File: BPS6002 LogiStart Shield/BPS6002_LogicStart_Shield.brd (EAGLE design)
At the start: 118.4 x 58.7 mm, 84 parts, among them J1 AUDIO-CONNECTOR-6P-SMD-344003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, Q1 MMBTA56, Q2 MMBTA56, Q3 MMBTA56, Q4 MMBTA56, Q5 MMBTA56

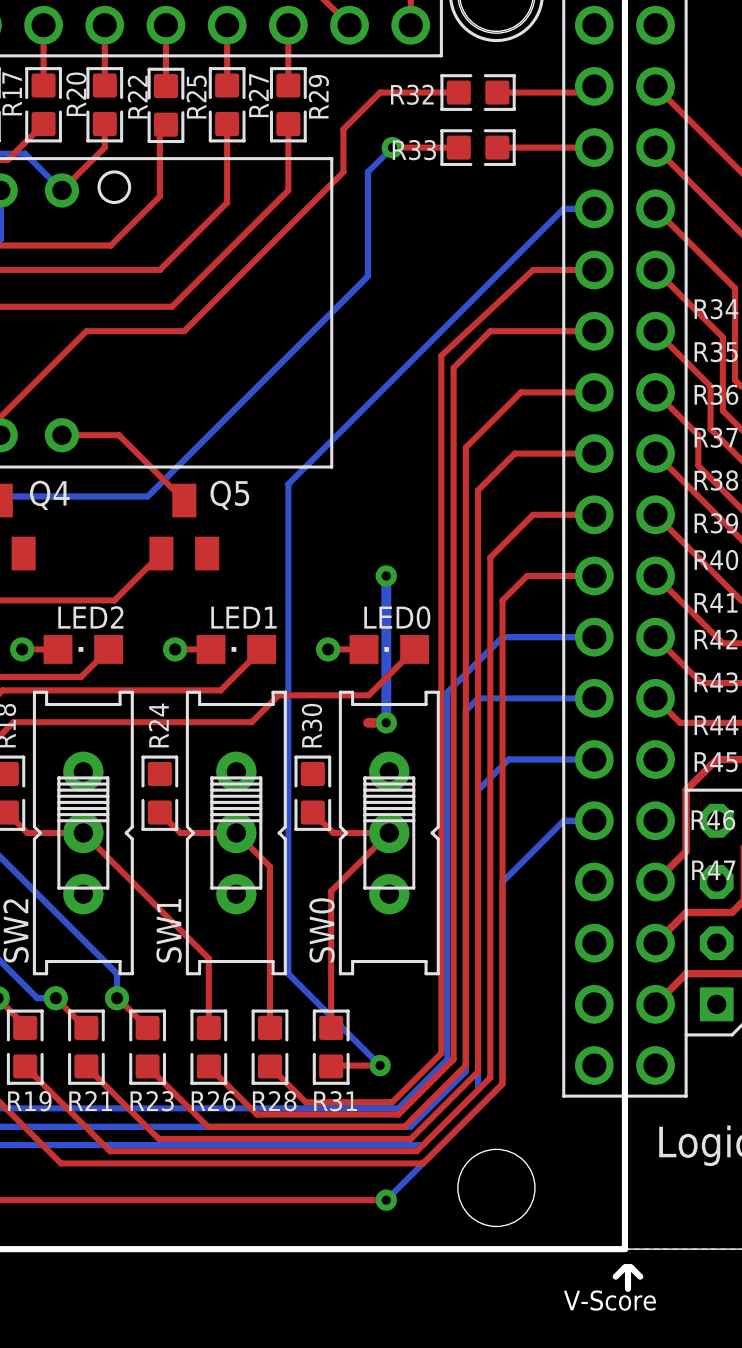
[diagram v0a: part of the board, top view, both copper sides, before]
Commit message: Added GPIO Header
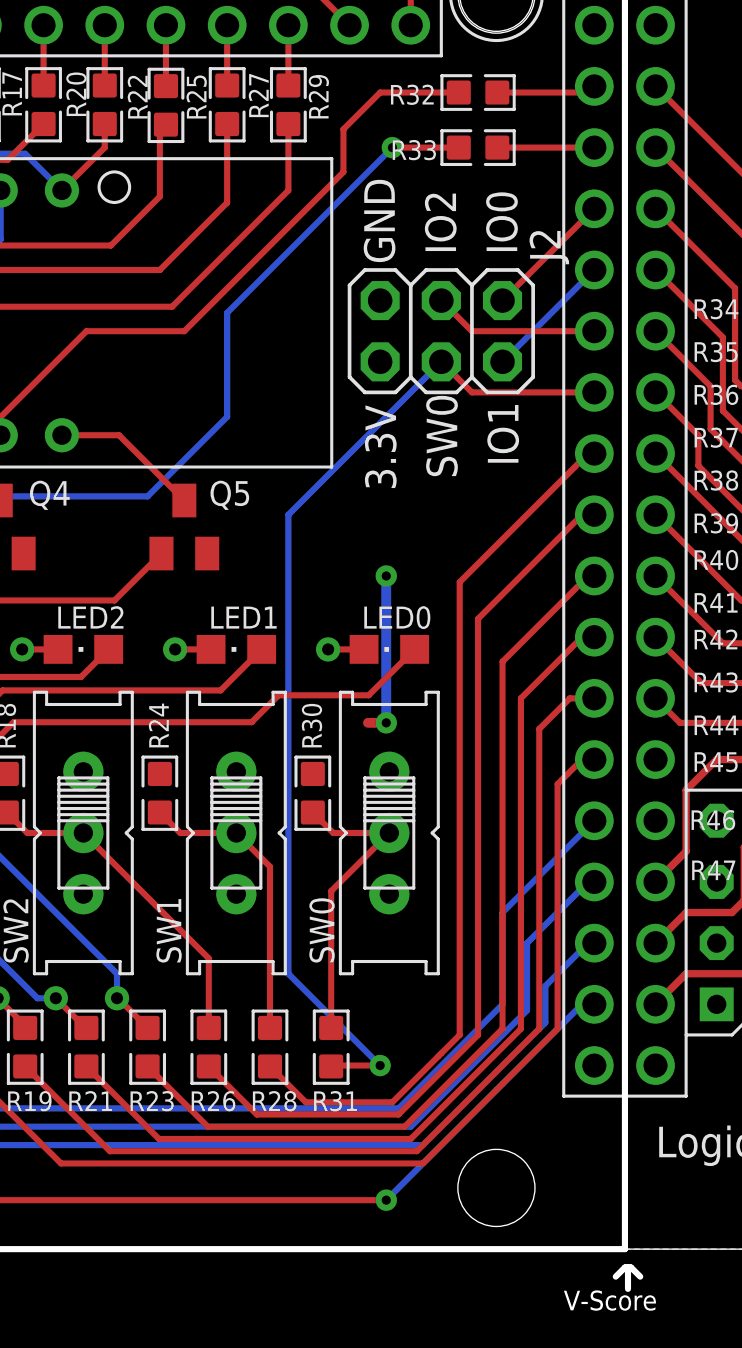
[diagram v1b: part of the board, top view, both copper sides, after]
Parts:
- added J2: (no value), pinhead:2X03
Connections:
- removed net NC1: H1.D48
- removed net NC2: H1.D50
- removed net NC3: H1.D52
- new net GPIO0: H1.D26, J2.1
- new net GPIO1: H1.D28, J2.2
- new net GPIO2: H1.D30, J2.3
- net 3V3: now also J2.6
- net GND: now also J2.5
- net LED0: now also H1.D48; no longer H1.D42
- net LED1: now also H1.D50; no longer H1.D44
- net LED2: now also H1.D52; no longer H1.D46
- net SW0: now also H1.D32, J2.4; no longer H1.D26
- net SW1: now also H1.D34; no longer H1.D28
- net SW2: now also H1.D36; no longer H1.D30
- net SW3: now also H1.D38; no longer H1.D32
- net SW4: now also H1.D40; no longer H1.D34
- net SW5: now also H1.D42; no longer H1.D36
- net SW6: now also H1.D44; no longer H1.D38
- net SW7: now also H1.D46; no longer H1.D40
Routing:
- net LED0: track 48.5 -> 38.2 mm
- net SW7: track 46.7 -> 36.9 mm
- net SW2: track 47.1 -> 37.3 mm
- net LED1: track 49.2 -> 39.6 mm
- net SW4: track 48.2 -> 39.0 mm
- net SW3: track 47.2 -> 38.0 mm
- net SW1: track 45.3 -> 36.2 mm
- net SW6: track 49.7 -> 40.7 mm
- net SW5: track 48.7 -> 40.2 mm
- net LED2: track 50.1 -> 42.0 mm
- net GPIO2: track 0.00 -> 6.88 mm
- net GPIO1: track 0.00 -> 5.39 mm
- net GPIO0: track 0.00 -> 5.39 mm
- net SW0: track 45.2 -> 42.3 mm
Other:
- board text added: "3.3V"
- board text added: "IO0"
- board text added: "IO1"
- board text added: "IO2"
- board text added: "SW0"

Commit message: LogicStart Shield with Joystick generic header
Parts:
- added J3: (no value), pinhead:2X03
- added R48, R49, R50, R51, R52: 390, GadgetFactory:0603
- moved R11 33.1 mm to (90.7, 10.2), turned to 0 degrees
- moved R12 30.8 mm to (90.7, 12.7), turned to 0 degrees
- moved R13 28.8 mm to (90.7, 15.2), turned to 0 degrees
- moved R15 28.3 mm to (37.8, 15.5)
- moved R16 24.7 mm to (44.2, 15.5)
- moved R19 21.0 mm to (50.5, 15.5)
- moved R21 17.5 mm to (56.9, 15.5)
- moved R23 14.1 mm to (63.2, 15.5)
- moved R26 11.0 mm to (69.6, 15.5)
- moved R28 8.45 mm to (75.9, 15.5)
- moved R31 7.15 mm to (82.3, 15.5)
- moved Q1 0.25 mm to (52.8, 30.2)
- moved Q2 0.25 mm to (56.6, 30.2)
- moved Q3 0.25 mm to (61.7, 30.2)
- moved Q4 0.25 mm to (69.3, 30.2)
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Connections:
- new net N$2: Q1.1, R48.1
- new net N$3: Q2.1, R49.1
- new net N$6: Q4.1, R50.1
- new net N$7: Q5.1, R51.1
- new net N$8: Q3.1, R52.1
- net AN0: now also H1.D40, R48.2; no longer H1.D3, Q1.1
- net AN1: now also H1.D38, R49.2; no longer H1.D2, Q2.1
- net AN2: now also H1.D34, R50.2; no longer H1.RX, Q4.1
- net AN3: now also H1.D32, R51.2; no longer H1.D4, Q5.1
- net AN4: now also H1.D36, R52.2; no longer H1.TX, Q3.1
- net DIR_DOWN: now also J3.4
- net DIR_LEFT: now also J3.3
- net DIR_RIGHT: now also J3.1
- net DIR_UP: now also J3.2
- net GND: now also J3.5
- net SW0: now also H1.RX; no longer H1.D32
- net SW1: now also H1.TX; no longer H1.D34
- net SW2: now also H1.D2; no longer H1.D36
- net SW3: now also H1.D3; no longer H1.D38
- net SW4: now also H1.D4; no longer H1.D40
- net SW7: now also J3.6
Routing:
- net SW7: track 36.9 -> 78.9 mm
- net N$2: track 0.00 -> 40.9 mm
- net LED2: track 42.0 -> 2.50 mm, vias 1 -> 0
- net AN3: track 52.1 -> 14.8 mm
- net LED1: track 39.6 -> 2.50 mm, vias 1 -> 0
- net N$3: track 0.00 -> 36.0 mm
- net LED0: track 38.2 -> 2.50 mm, vias 1 -> 0
- net N$8: track 0.00 -> 31.6 mm
- net AN2: track 34.2 -> 3.45 mm, vias 1 -> 0
- net DIR_LEFT: track 39.7 -> 69.8 mm
- net SW1: track 36.2 -> 65.5 mm, vias 0 -> 1
- net AN4: track 31.1 -> 3.24 mm
- net SW7_IN: track 31.1 -> 4.86 mm, vias 1 -> 0
- net SW6: track 40.7 -> 66.1 mm, vias 0 -> 1
- net AN1: track 28.2 -> 3.03 mm
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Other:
- board text added: "Down"
- board text added: "Fire"
- board text added: "Left"
- board text added: "Right"
- board text added: "Up"

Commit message: LogicStart Shield
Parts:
- removed J3: (no value), pinhead:2X03
- added W1: WING8_NOHOLES_FEMALE_TOP, Papilio:WINGSIDE_8BIT_NOHOLES
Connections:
- net 3V3: now also W1.3V3@2
- net 5V0: now also W1.5V@2
- net DIR_DOWN: no longer J3.4
- net DIR_LEFT: no longer J3.3
- net DIR_RIGHT: no longer J3.1
- net DIR_UP: no longer J3.2
- net GND: now also W1.GND@2; no longer J3.5
- net SW0: now also W1.7
- net SW1: now also W1.6
- net SW2: now also W1.5
- net SW3: now also W1.4
- net SW4: now also W1.3
- net SW5: now also W1.2
- net SW6: now also W1.1
- net SW7: now also W1.0; no longer J3.6
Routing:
- net 5V0: track 95.0 -> 135.6 mm, vias 1 -> 3
- net DIR_LEFT: track 69.8 -> 39.7 mm
- net SW4: track 45.4 -> 67.9 mm
- net DIR_UP: track 52.5 -> 31.9 mm, vias 1 -> 0
- net SW3: track 54.6 -> 72.1 mm
- net SW2: track 58.7 -> 71.5 mm
- net SW1: track 65.5 -> 76.0 mm
- net DIR_RIGHT: track 43.9 -> 33.4 mm
- net DIR_DOWN: track 64.1 -> 53.7 mm
- net SW0: track 67.0 -> 74.9 mm
- net SW5: track 59.5 -> 66.5 mm, vias 1 -> 0
- net SW7: track 78.9 -> 73.7 mm
- net A2: track 37.4 -> 39.9 mm
- net A3: track 46.4 -> 47.8 mm
- net SW6: track 66.1 -> 67.1 mm, vias 1 -> 2
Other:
- outline, holes or cut-outs redrawn
- board text added: "WING1"
- board text removed: "Down"
- board text removed: "Fire"
- board text removed: "Left"
- board text removed: "Right"
- board text removed: "Up"
